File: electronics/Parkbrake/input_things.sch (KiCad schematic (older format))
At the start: 11 parts

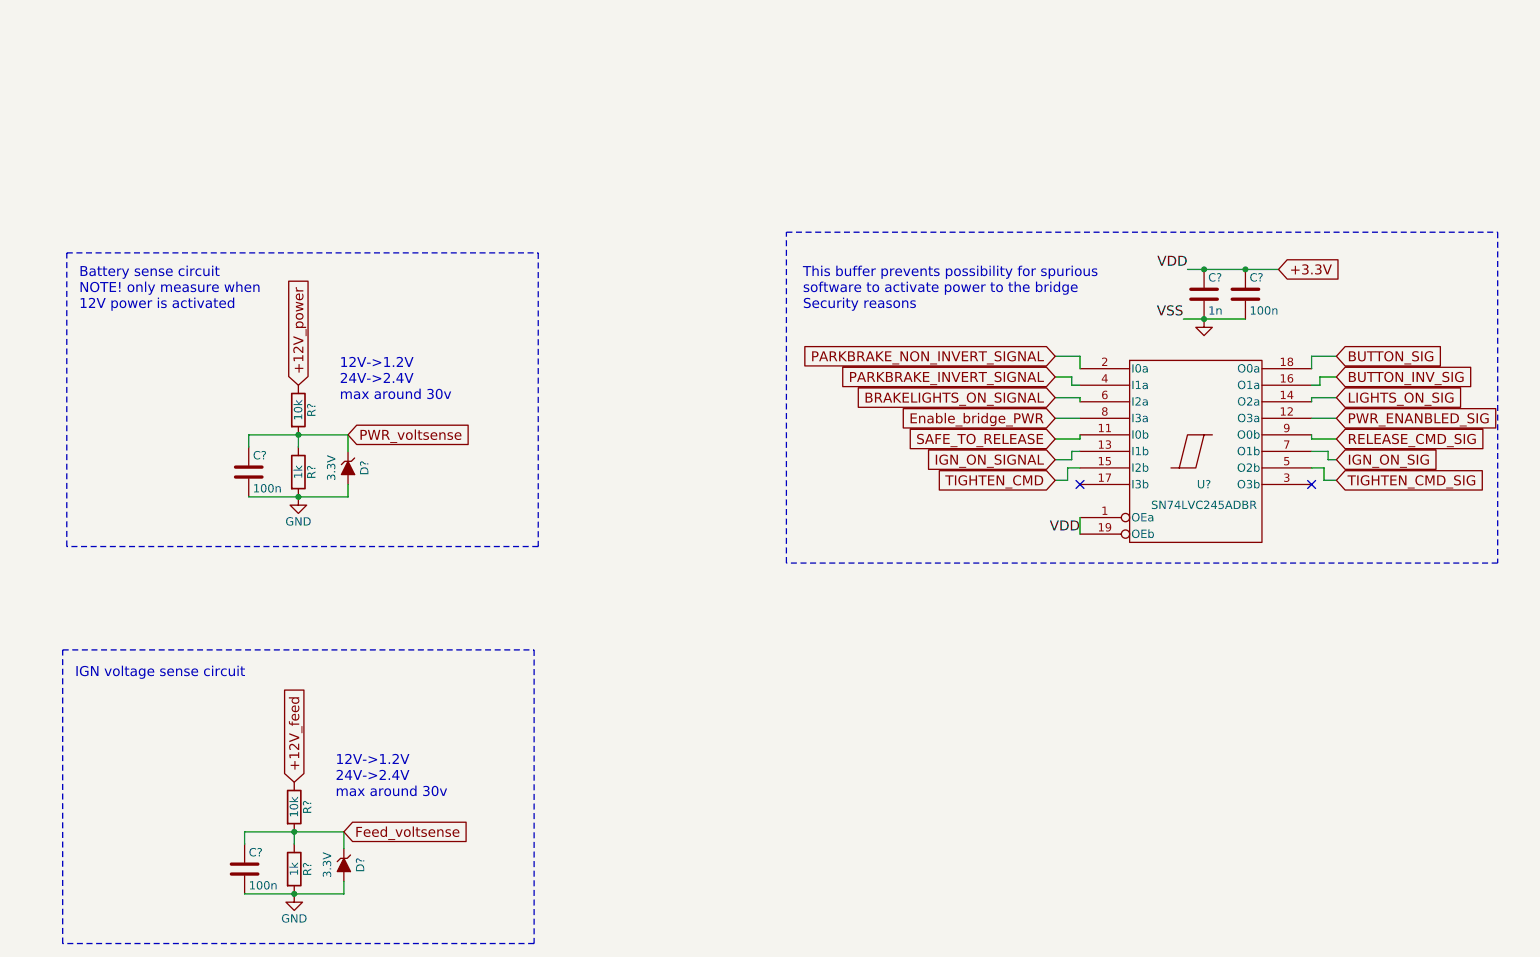
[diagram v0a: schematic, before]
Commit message: ordernr, type and footprints for all components
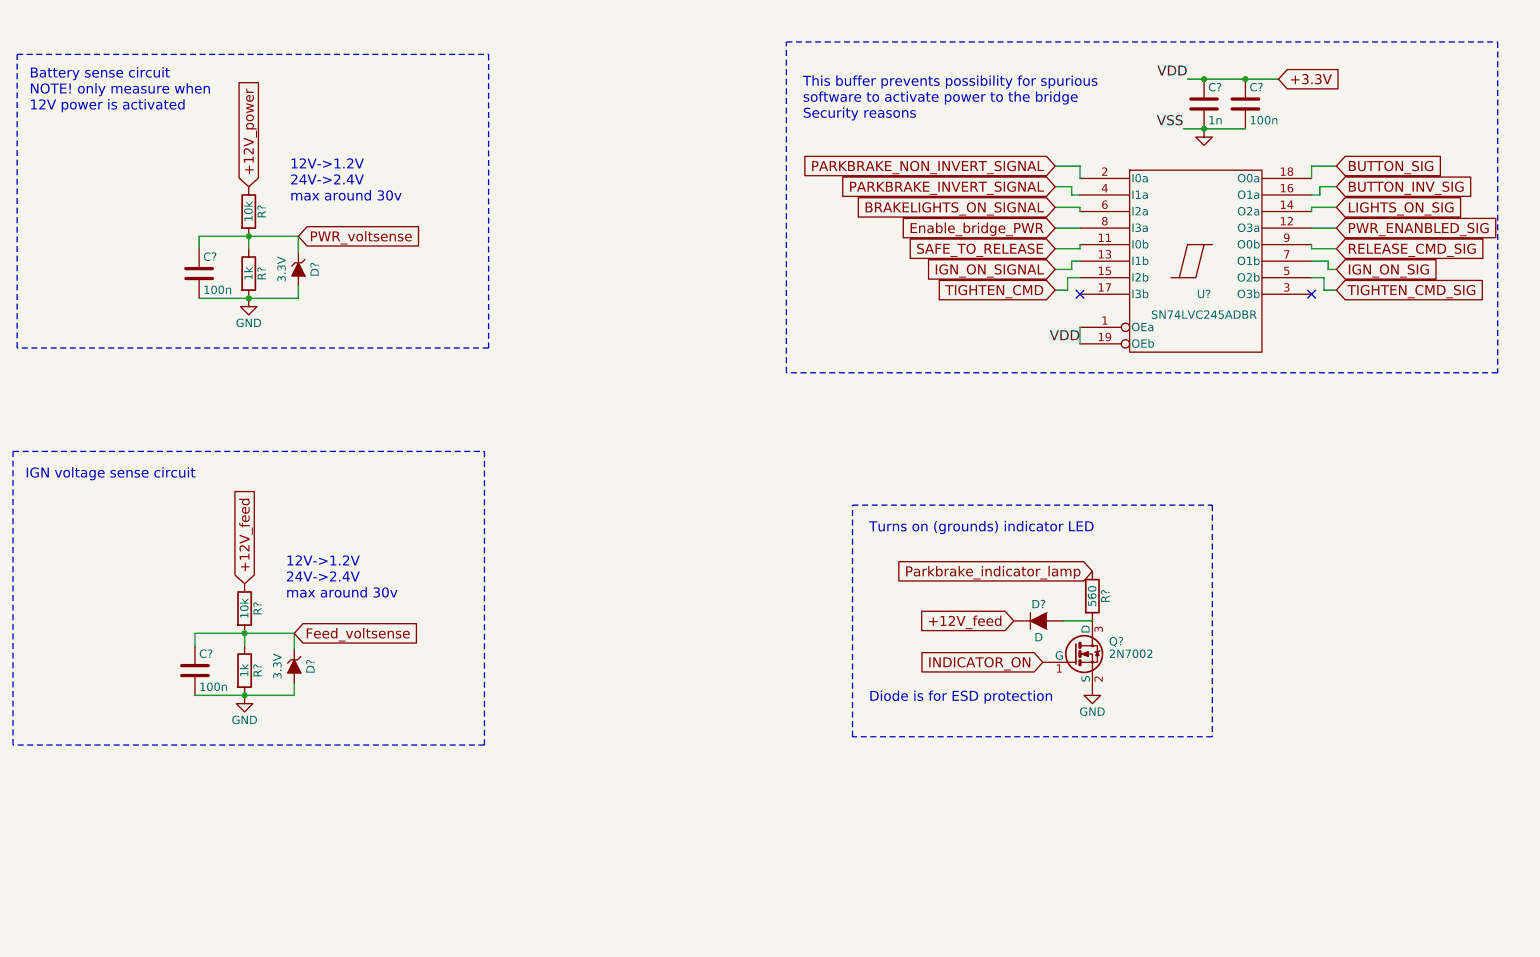
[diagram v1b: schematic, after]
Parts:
- added D?: D, symbol D
- added Q?: 2N7002, TO_SOT_Packages_SMD:SOT-23, symbol BSS138
- added R?: 560, Resistors_SMD:R_0805, symbol R
- C?: footprint (none) -> Capacitors_SMD:C_0805; farnell (none) -> 2494247; part (none) -> GRM2165C1H102JA01D
- C? (x3): farnell (none) -> 2496940; part (none) -> 0805B104J500CT
- D? (x2): footprint (none) -> Diodes_SMD:SOD-123; farnell (none) -> 2454044; part (none) -> MMSZ4684
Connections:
- net +12V_feed: now also D?.1 (K)
- net GND: now also Q?.2 (S)
- new net: D?.2 (A), Q?.3 (D), R?.2
- new net INDICATOR_ON: Q?.1 (G)
- new net Parkbrake_indicator_lamp: R?.1
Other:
- note added: "Diode is for ESD protection"
- note added: "Turns on (grounds) indicator LED"
- moved on the sheet: C?, D?, R?, U?

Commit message: Make it pass DRC rule check
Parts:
- gave numbers to parts that had none: 14
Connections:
- net Enable_bridge_PWR renamed Enable_Bridge_PWR
- net PARKBRAKE_INVERT_SIGNAL renamed ~PARKBRAKE_INVERT_SIGNAL
- net PWR_ENANBLED_SIG renamed PWR_ENABLED_SIG
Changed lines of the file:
@@
 PARKBRAKE_NON_INVERT_SIGNAL
 Text GLabel 7500 2350 0    60   Input ~ 0
-PARKBRAKE_INVERT_SIGNAL
+~PARKBRAKE_INVERT_SIGNAL
 Text GLabel 7500 2975 0    60   Input ~ 0
 TIGHTEN_CMD
@@
 SAFE_TO_RELEASE
 Text GLabel 7500 2600 0    60   Input ~ 0
-Enable_bridge_PWR
-$Comp
-L C C?
+Enable_Bridge_PWR
+$Comp
+L C C63
 U 1 1 5793D998
 P 8400 1850
-F 0 "C?" H 8425 1950 50  0000 L CNN
+F 0 "C63" H 8425 1950 50  0000 L CNN
 F 1 "1n" H 8425 1750 50  0000 L CNN
 F 2 "Capacitors_SMD:C_0805" H 8438 1700 50  0001 C CNN
@@
 $EndComp
 $Comp
-L C C?
+L C C64
 U 1 1 5793D9CB
 P 8650 1850
-F 0 "C?" H 8675 1950 50  0000 L CNN
+F 0 "C64" H 8675 1950 50  0000 L CNN
 F 1 "100n" H 8675 1750 50  0000 L CNN
 F 2 "" H 8688 1700 50  0000 C CNN
@@
 $EndComp
 $Comp
-L GND #PWR?
+L GND #PWR089
 U 1 1 5793D9FE
 P 8400 2000
-F 0 "#PWR?" H 8400 1750 50  0001 C CNN
+F 0 "#PWR089" H 8400 1750 50  0001 C CNN
 F 1 "GND" H 8400 1850 50  0001 C CNN
 F 2 "" H 8400 2000 50  0000 C CNN
@@
 +3.3V
 $Comp
-L 74LS241 U?
+L 74LS241 U27
 U 1 1 5793E341
 P 8350 2800
-F 0 "U?" H 8400 2600 50  0000 C CNN
+F 0 "U27" H 8400 2600 50  0000 C CNN
 F 1 "SN74LVC245ADBR" H 8400 2475 50  0000 C CNN
 F 2 "Housings_SSOP:SSOP-20_5.3x7.2mm_Pitch0.65mm" H 8350 2800 50  0001 C CNN
@@
 NoConn ~ 7650 3000
 $Comp
-L R R?
+L R R102
 U 1 1 5793F16C
 P 2625 2500
-F 0 "R?" V 2705 2500 50  0000 C CNN
+F 0 "R102" V 2705 2500 50  0000 C CNN
 F 1 "10k" V 2625 2500 50  0000 C CNN
 F 2 "Resistors_SMD:R_0805" V 2555 2500 50  0001 C CNN
@@
 $EndComp
 $Comp
-L R R?
+L R R103
 U 1 1 5793F18B
 P 2625 2875
-F 0 "R?" V 2705 2875 50  0000 C CNN
+F 0 "R103" V 2705 2875 50  0000 C CNN
 F 1 "1k" V 2625 2875 50  0000 C CNN
 F 2 "Resistors_SMD:R_0805" V 2555 2875 50  0001 C CNN
@@
 $EndComp
 $Comp
-L C C?
+L C C62
 U 1 1 5793F1C0
 P 2325 2875
-F 0 "C?" H 2350 2975 50  0000 L CNN
+F 0 "C62" H 2350 2975 50  0000 L CNN
 F 1 "100n" H 2350 2775 50  0000 L CNN
 F 2 "" H 2363 2725 50  0000 C CNN
@@
 $EndComp
 $Comp
-L ZENERsmall D?
+L ZENERsmall D27
 U 1 1 5793F24E
 P 2925 2850
-F 0 "D?" H 2925 2950 50  0000 C CNN
+F 0 "D27" H 2925 2950 50  0000 C CNN
 F 1 "3.3V" H 2925 2750 50  0000 C CNN
 F 2 "Diodes_SMD:SOD-123" H 2925 2850 50  0001 C CNN
@@
 +12V_power
 $Comp
-L GND #PWR?
+L GND #PWR090
 U 1 1 5793F3F6
 P 2625 3025
-F 0 "#PWR?" H 2625 2775 50  0001 C CNN
+F 0 "#PWR090" H 2625 2775 50  0001 C CNN
 F 1 "GND" H 2625 2875 50  0000 C CNN
 F 2 "" H 2625 3025 50  0000 C CNN
@@
 LIGHTS_ON_SIG
 Text GLabel 9200 2600 2    60   Input ~ 0
-PWR_ENANBLED_SIG
+PWR_ENABLED_SIG
 Text GLabel 9200 2725 2    60   Input ~ 0
 RELEASE_CMD_SIG
@@
 	5875 3475 5875 1475
 $Comp
-L R R?
+L R R100
 U 1 1 57945BE0
 P 2600 4900
-F 0 "R?" V 2680 4900 50  0000 C CNN
+F 0 "R100" V 2680 4900 50  0000 C CNN
 F 1 "10k" V 2600 4900 50  0000 C CNN
 F 2 "" V 2530 4900 50  0000 C CNN
@@
 $EndComp
 $Comp
-L R R?
+L R R101
 U 1 1 57945BE6
 P 2600 5275
-F 0 "R?" V 2680 5275 50  0000 C CNN
+F 0 "R101" V 2680 5275 50  0000 C CNN
 F 1 "1k" V 2600 5275 50  0000 C CNN
 F 2 "Resistors_SMD:R_0805" V 2530 5275 50  0001 C CNN
@@
 $EndComp
 $Comp
-L C C?
+L C C61
 U 1 1 57945BEC
 P 2300 5275
-F 0 "C?" H 2325 5375 50  0000 L CNN
+F 0 "C61" H 2325 5375 50  0000 L CNN
 F 1 "100n" H 2325 5175 50  0000 L CNN
 F 2 "" H 2338 5125 50  0000 C CNN
@@
 $EndComp
 $Comp
-L ZENERsmall D?
+L ZENERsmall D26
 U 1 1 57945BF2
 P 2900 5250
-F 0 "D?" H 2900 5350 50  0000 C CNN
+F 0 "D26" H 2900 5350 50  0000 C CNN
 F 1 "3.3V" H 2900 5150 50  0000 C CNN
 F 2 "Diodes_SMD:SOD-123" H 2900 5250 50  0001 C CNN
@@
 +12V_feed
 $Comp
-L GND #PWR?
+L GND #PWR091
 U 1 1 57945BF9
 P 2600 5425
-F 0 "#PWR?" H 2600 5175 50  0001 C CNN
+F 0 "#PWR091" H 2600 5175 50  0001 C CNN
 F 1 "GND" H 2600 5275 50  0000 C CNN
 F 2 "" H 2600 5425 50  0000 C CNN
@@
 	1200 5725 1200 3950
 $Comp
-L R R?
+L R R104
 U 1 1 579422D1
 P 7725 4825
-F 0 "R?" V 7805 4825 50  0000 C CNN
+F 0 "R104" V 7805 4825 50  0000 C CNN
 F 1 "560" V 7725 4825 50  0000 C CNN
 F 2 "Resistors_SMD:R_0805" V 7655 4825 50  0001 C CNN
@@
 $EndComp
 $Comp
-L BSS138 Q?
+L BSS138 Q38
 U 1 1 57942372
 P 7625 5175
-F 0 "Q?" H 7825 5250 50  0000 L CNN
+F 0 "Q38" H 7825 5250 50  0000 L CNN
 F 1 "2N7002" H 7825 5175 50  0000 L CNN
 F 2 "TO_SOT_Packages_SMD:SOT-23" H 7825 5100 50  0001 L CIN
@@
 $EndComp
 $Comp
-L GND #PWR?
+L GND #PWR092
 U 1 1 57942417
 P 7725 5375
-F 0 "#PWR?" H 7725 5125 50  0001 C CNN
+F 0 "#PWR092" H 7725 5125 50  0001 C CNN
 F 1 "GND" H 7725 5225 50  0000 C CNN
 F 2 "" H 7725 5375 50  0000 C CNN
@@
 	6275 5675 6275 4275
 $Comp
-L D D?
+L D D28
 U 1 1 5794388E
 P 7400 4975
-F 0 "D?" H 7400 5075 50  0000 C CNN
+F 0 "D28" H 7400 5075 50  0000 C CNN
 F 1 "D" H 7400 4875 50  0000 C CNN
 F 2 "" H 7400 4975 50  0000 C CNN

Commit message: More fixes and chenged components eat less boardspace
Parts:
- C61, C62, C64: footprint (none) -> Capacitors_SMD:C_0805
- D28: renamed from D26; footprint Diodes_SMD:SOD-123 -> Diodes_SMD:SOD-323; farnell 2454044 -> 2463489; part MMSZ4684 -> MM3Z3V3ST1G
- D29: renamed from D27; footprint Diodes_SMD:SOD-123 -> Diodes_SMD:SOD-323; farnell 2454044 -> 2463489; part MMSZ4684 -> MM3Z3V3ST1G
- D30: renamed from D28; value D -> 1n4148w; footprint (none) -> Diodes_SMD:SOD-323; farnell (none) -> 1466524; part (none) -> 1N4148WS
- Q31: renamed from Q38; value 2N7002 -> BSS138; footprint TO_SOT_Packages_SMD:SOT-23 -> TO_SOT_Packages_SMD:SOT-323; farnell 1510761 -> 1907611; part 2N7002 -> BSS138PW
- R98: renamed from R100; footprint (none) -> Resistors_SMD:R_0805
- renumbered R102 to R100, R103 to R101, R104 to R102, R101 to R99
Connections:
- net +12V_power renamed +12V_powerFront
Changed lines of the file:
@@
 F 0 "C64" H 8675 1950 50  0000 L CNN
 F 1 "100n" H 8675 1750 50  0000 L CNN
-F 2 "" H 8688 1700 50  0000 C CNN
+F 2 "Capacitors_SMD:C_0805" H 8688 1700 50  0001 C CNN
 F 3 "" H 8650 1850 50  0000 C CNN
 F 4 "0805B104J500CT" H 8650 1850 60  0001 C CNN "part"
@@
 $EndComp
 $Comp
-L GND #PWR089
+L GND #PWR85
 U 1 1 5793D9FE
 P 8400 2000
-F 0 "#PWR089" H 8400 1750 50  0001 C CNN
+F 0 "#PWR85" H 8400 1750 50  0001 C CNN
 F 1 "GND" H 8400 1850 50  0001 C CNN
 F 2 "" H 8400 2000 50  0000 C CNN
@@
 NoConn ~ 7650 3000
 $Comp
-L R R102
+L R R100
 U 1 1 5793F16C
 P 2625 2500
-F 0 "R102" V 2705 2500 50  0000 C CNN
+F 0 "R100" V 2705 2500 50  0000 C CNN
 F 1 "10k" V 2625 2500 50  0000 C CNN
 F 2 "Resistors_SMD:R_0805" V 2555 2500 50  0001 C CNN
@@
 $EndComp
 $Comp
-L R R103
+L R R101
 U 1 1 5793F18B
 P 2625 2875
-F 0 "R103" V 2705 2875 50  0000 C CNN
+F 0 "R101" V 2705 2875 50  0000 C CNN
 F 1 "1k" V 2625 2875 50  0000 C CNN
 F 2 "Resistors_SMD:R_0805" V 2555 2875 50  0001 C CNN
@@
 F 0 "C62" H 2350 2975 50  0000 L CNN
 F 1 "100n" H 2350 2775 50  0000 L CNN
-F 2 "" H 2363 2725 50  0000 C CNN
+F 2 "Capacitors_SMD:C_0805" H 2363 2725 50  0001 C CNN
 F 3 "" H 2325 2875 50  0000 C CNN
 F 4 "0805B104J500CT" H 2325 2875 60  0001 C CNN "part"
@@
 $EndComp
 $Comp
-L ZENERsmall D27
+L ZENERsmall D29
 U 1 1 5793F24E
 P 2925 2850
-F 0 "D27" H 2925 2950 50  0000 C CNN
+F 0 "D29" H 2925 2950 50  0000 C CNN
 F 1 "3.3V" H 2925 2750 50  0000 C CNN
-F 2 "Diodes_SMD:SOD-123" H 2925 2850 50  0001 C CNN
+F 2 "Diodes_SMD:SOD-323" H 2925 2850 50  0001 C CNN
 F 3 "" H 2925 2850 50  0000 C CNN
-F 4 "MMSZ4684" H 2925 2850 60  0001 C CNN "part"
-F 5 "2454044" H 2925 2850 60  0001 C CNN "farnell"
+F 4 "MM3Z3V3ST1G" H 2925 2850 60  0001 C CNN "part"
+F 5 "2463489" H 2925 2850 60  0001 C CNN "farnell"
 	1    2925 2850
 	0    1    1    0
 $EndComp
 Text GLabel 2625 2350 1    60   Input ~ 0
-+12V_power
-$Comp
-L GND #PWR090
++12V_powerFront
+$Comp
+L GND #PWR83
 U 1 1 5793F3F6
 P 2625 3025
-F 0 "#PWR090" H 2625 2775 50  0001 C CNN
+F 0 "#PWR83" H 2625 2775 50  0001 C CNN
 F 1 "GND" H 2625 2875 50  0000 C CNN
 F 2 "" H 2625 3025 50  0000 C CNN
@@
 	2325 2650 2325 2725
 Connection ~ 2625 2650
-Text Notes 1300 1900 0    60   ~ 0
+Text Notes 1300 1750 0    60   ~ 0
 Battery sense circuit\nNOTE! only measure when \n12V power is activated
 Text Notes 2875 2450 0    60   ~ 0
 12V->1.2V \n24V->2.4V\nmax around 30v
 Wire Notes Line
-	1225 1550 4075 1550
-Wire Notes Line
-	4075 1550 4075 3325
+	1225 1425 4075 1425
+Wire Notes Line
+	4075 1425 4075 3325
 Wire Notes Line
 	4075 3325 1225 3325
 Wire Notes Line
-	1225 3325 1225 1550
+	1225 3325 1225 1425
 Text GLabel 9200 2225 2    60   Input ~ 0
 BUTTON_SIG
@@
 	5875 3475 5875 1475
 $Comp
-L R R100
+L R R98
 U 1 1 57945BE0
 P 2600 4900
-F 0 "R100" V 2680 4900 50  0000 C CNN
+F 0 "R98" V 2680 4900 50  0000 C CNN
 F 1 "10k" V 2600 4900 50  0000 C CNN
-F 2 "" V 2530 4900 50  0000 C CNN
+F 2 "Resistors_SMD:R_0805" V 2530 4900 50  0001 C CNN
 F 3 "" H 2600 4900 50  0000 C CNN
 F 4 "MC01W0805110K" V 2600 4900 60  0001 C CNN "part"
@@
 $EndComp
 $Comp
-L R R101
+L R R99
 U 1 1 57945BE6
 P 2600 5275
-F 0 "R101" V 2680 5275 50  0000 C CNN
+F 0 "R99" V 2680 5275 50  0000 C CNN
 F 1 "1k" V 2600 5275 50  0000 C CNN
 F 2 "Resistors_SMD:R_0805" V 2530 5275 50  0001 C CNN
@@
 F 0 "C61" H 2325 5375 50  0000 L CNN
 F 1 "100n" H 2325 5175 50  0000 L CNN
-F 2 "" H 2338 5125 50  0000 C CNN
+F 2 "Capacitors_SMD:C_0805" H 2338 5125 50  0001 C CNN
 F 3 "" H 2300 5275 50  0000 C CNN
 F 4 "0805B104J500CT" H 2300 5275 60  0001 C CNN "part"
@@
 $EndComp
 $Comp
-L ZENERsmall D26
+L ZENERsmall D28
 U 1 1 57945BF2
 P 2900 5250
-F 0 "D26" H 2900 5350 50  0000 C CNN
+F 0 "D28" H 2900 5350 50  0000 C CNN
 F 1 "3.3V" H 2900 5150 50  0000 C CNN
-F 2 "Diodes_SMD:SOD-123" H 2900 5250 50  0001 C CNN
+F 2 "Diodes_SMD:SOD-323" H 2900 5250 50  0001 C CNN
 F 3 "" H 2900 5250 50  0000 C CNN
-F 4 "2454044" H 2900 5250 60  0001 C CNN "farnell"
-F 5 "MMSZ4684" H 2900 5250 60  0001 C CNN "part"
+F 4 "2463489" H 2900 5250 60  0001 C CNN "farnell"
+F 5 "MM3Z3V3ST1G" H 2900 5250 60  0001 C CNN "part"
 	1    2900 5250
 	0    1    1    0
@@
 +12V_feed
 $Comp
-L GND #PWR091
+L GND #PWR82
 U 1 1 57945BF9
 P 2600 5425
-F 0 "#PWR091" H 2600 5175 50  0001 C CNN
+F 0 "#PWR82" H 2600 5175 50  0001 C CNN
 F 1 "GND" H 2600 5275 50  0000 C CNN
 F 2 "" H 2600 5425 50  0000 C CNN
@@
 	1200 5725 1200 3950
 $Comp
-L R R104
+L R R102
 U 1 1 579422D1
 P 7725 4825
-F 0 "R104" V 7805 4825 50  0000 C CNN
+F 0 "R102" V 7805 4825 50  0000 C CNN
 F 1 "560" V 7725 4825 50  0000 C CNN
 F 2 "Resistors_SMD:R_0805" V 7655 4825 50  0001 C CNN
@@
 $EndComp
 $Comp
-L BSS138 Q38
+L BSS138 Q31
 U 1 1 57942372
 P 7625 5175
-F 0 "Q38" H 7825 5250 50  0000 L CNN
-F 1 "2N7002" H 7825 5175 50  0000 L CNN
-F 2 "TO_SOT_Packages_SMD:SOT-23" H 7825 5100 50  0001 L CIN
+F 0 "Q31" H 7825 5250 50  0000 L CNN
+F 1 "BSS138" H 7825 5175 50  0000 L CNN
+F 2 "TO_SOT_Packages_SMD:SOT-323" H 7825 5100 50  0001 L CIN
 F 3 "" H 7625 5175 50  0000 L CNN
-F 4 "2N7002" H 7625 5175 60  0001 C CNN "part"
-F 5 "1510761" H 7625 5175 60  0001 C CNN "farnell"
+F 4 "BSS138PW" H 7625 5175 60  0001 C CNN "part"
+F 5 "1907611" H 7625 5175 60  0001 C CNN "farnell"
 	1    7625 5175
 	1    0    0    -1
 $EndComp
 $Comp
-L GND #PWR092
+L GND #PWR84
 U 1 1 57942417
 P 7725 5375
-F 0 "#PWR092" H 7725 5125 50  0001 C CNN
+F 0 "#PWR84" H 7725 5125 50  0001 C CNN
 F 1 "GND" H 7725 5225 50  0000 C CNN
 F 2 "" H 7725 5375 50  0000 C CNN
@@
 	6275 5675 6275 4275
 $Comp
-L D D28
+L D D30
 U 1 1 5794388E
 P 7400 4975
-F 0 "D28" H 7400 5075 50  0000 C CNN
-F 1 "D" H 7400 4875 50  0000 C CNN
-F 2 "" H 7400 4975 50  0000 C CNN
+F 0 "D30" H 7400 5075 50  0000 C CNN
+F 1 "1n4148w" H 7400 4875 50  0000 C CNN
+F 2 "Diodes_SMD:SOD-323" H 7400 4975 50  0001 C CNN
 F 3 "" H 7400 4975 50  0000 C CNN
+F 4 "1466524" H 7400 4975 60  0001 C CNN "farnell"
+F 5 "1N4148WS" H 7400 4975 60  0001 C CNN "part"
 	1    7400 4975
 	1    0    0    -1
